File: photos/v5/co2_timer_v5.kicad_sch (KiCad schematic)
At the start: 57 parts, among them J1 BAT1_9V, J2 SOLENOID, J3 AVR-ISP-6 (DNP prod), J4 TM1637_DISPLAY, J5 DC_9-12V, J6 BAT2_9V, SW1 UP, SW2 SET, U1 ATtiny84A-SSU, U2 DS3231M+TRL, U3 MCP1703A-3302E/CB, U4 DRV8871DDAR, U5 TPS3839G30DBZR, U6 SN74LVC1G123DCUR

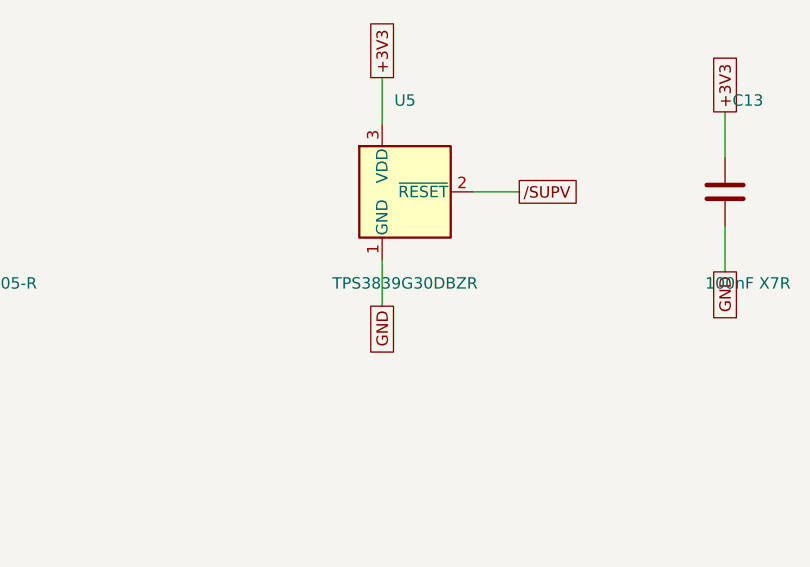
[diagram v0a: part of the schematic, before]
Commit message: docs(co2-timer): v5 fab package and firmware doc refresh
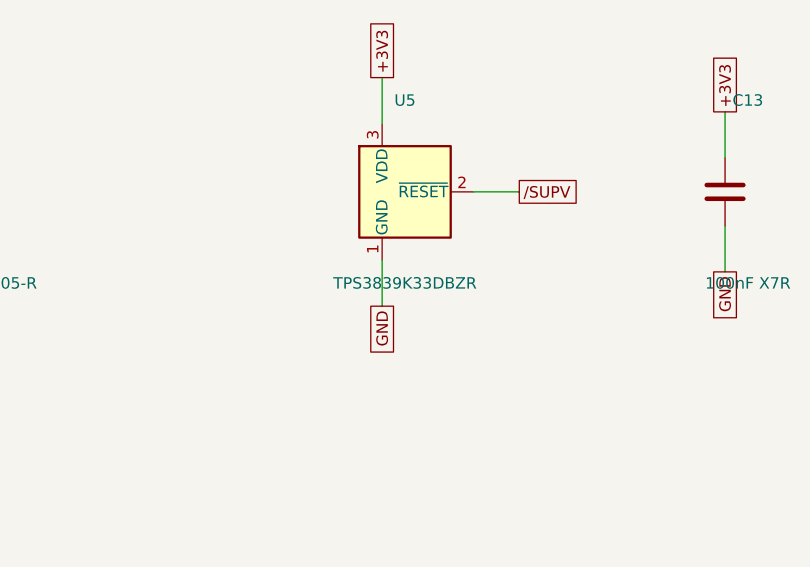
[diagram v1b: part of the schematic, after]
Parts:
- U5: value TPS3839G30DBZR -> TPS3839K33DBZR
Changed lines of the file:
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@@
 			(effects (font (size 1.27 1.27)))
 		)
-		(property "Value" "TPS3839G30DBZR"
+		(property "Value" "TPS3839K33DBZR"
 			(at 345.44 193.04 0)
 			(effects (font (size 1.27 1.27)))

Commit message: co2-timer v5.1: fail-safe redesign + full adversarial remediation
Adversarial review (2026-08-11) found the shipped-for-quote package had a
reversed regulator pinout, a fail-safe chain that could not actuate (supervisor
tripped 3.5 V below bridge UVLO; one-shot mistimed and self-powered; 470 uF
reservoir off by 100x), unmountable C1/SC1/diode footprints, and no valve spec.

Rev 5.1, verified through six adversarial re-review rounds to RELEASE:
- TPS3700 supervisor on VM (180K/10K, trip 7.50 V) + dual SN74LVC1G3157 muxes
  force IN1=0/IN2=1 at the bridge on trip; one-shot/diode-OR deleted
- U3 MCP1703A pad nets corrected everywhere incl. pad oracle and symbol
- C1 -> 2x 1000 uF D10/P5.0 (sag support role); SC1 -> 0.1 F coin (CHP5R5L104R);
  D2/D3 SOD-323 lands; BOM/CPL/netlist/oracle consistent (172/172)
- Firmware safety items 1-11: OSF masks, periodic schedule eval, close-on-reset
  + hop rescue w/ hold release on clean pass, tear-safe complement journal with
  break-count validation, BCD validation, sticky faults, 8.2/8.6 V lockout with
  .noinit latch + sleep-hop release, VM-measured alert classification
  (6,492 B, sha256 64b0808e...4453, compiled arduino-cli/ATTinyCore on gg-wsl)
- Valve: leak-qualified 6 V direct-acting micro latching class, MPN frozen at
  FA T0; dummy loads derived from measured coil; enclosure stays 1554C2GY
- Docs: T0-T8 + G1-G3 test series, ENIG finish, regulated-adapter constraint,
  Bittele 100-unit/5-FA-hold scope, fab package rebuilt with production hex
  + SHA256SUMS
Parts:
- removed C13, C8: 100nF X7R, Capacitor_SMD:C_0603_1608Metric, symbol Device:C
- removed D6: BAT54, Package_TO_SOT_SMD:SOT-23, symbol Device:D_Schottky
- removed U5: TPS3839K33DBZR, Package_TO_SOT_SMD:SOT-23, symbol Power_Supervisor:TPS3839DBZ
- removed U6: SN74LVC1G123DCUR, Package_SO:VSSOP-8_2.3x2mm_P0.5mm, symbol 74xGxx:74LVC1G123
- added C18: 100nF X7R, Capacitor_SMD:C_0603_1608Metric, symbol Device:C
- added C19: 1000uF 25V 105C low-ESR, Capacitor_THT:CP_Radial_D10.0mm_P5.00mm, symbol Device:C_Polarized
- added R17: 100K, Resistor_SMD:R_0603_1608Metric, symbol Device:R
- added R18: 10K, Resistor_SMD:R_0603_1608Metric, symbol Device:R
- added U5: TPS3700DDCR, Package_TO_SOT_SMD:SOT-23-6, symbol co2v5:TPS3700DDCR
- added U6, U7: SN74LVC1G3157DCKR, Package_TO_SOT_SMD:SOT-363_SC-70-6, symbol co2v5:SN74LVC1G3157
- C1: value 470uF 16V 105C low-ESR -> 1000uF 25V 105C low-ESR
- C9: value 470nF X7R -> 100nF X7R
- D2, D3: footprint Package_TO_SOT_SMD:SOT-23 -> Diode_SMD:D_SOD-323
- J5: footprint Connector_BarrelJack:BarrelJack_Horizontal -> co2v5:BarrelJack_CUI_PJ-002A
- R13: value 100K 1% -> 180K 1%
- R16: value 1K -> 10K 1%
- SC1: value 1F 5.5V PB-5R0V105-R -> 0.1F 5.5V CHP5R5L104R-TW; footprint Capacitor_THT:CP_Radial_D10.0mm_P5.00mm -> co2v5:CP_CHP_10x5_P7.50mm
- SW1, SW2: footprint Button_Switch_SMD:SW_SPST_TL3342 -> co2v5:PTS645SM43SMTR92LFS
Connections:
- net OS_CEXT is gone; now on net VM: C9.1
- net +3V3: now also U3.2 (VOUT), C18.1, R18.2, U6.5 (VCC), U7.3 (B1), U7.5 (VCC); no longer R13.2, U3.3 (VOUT)
- net DRV_IN1: now also U6.4 (A); no longer U1.2 (XTAL1/PB0)
- net DRV_IN2: now also U7.4 (A); no longer R16.2
- net DRV_IN2_MCU: now also U7.1 (B2); no longer R16.1
- net GND: now also C9.2, R16.2, C18.2, C19.2, R17.2, U5.2 (GND), U5.4 (INB-), U6.2 (GND), U6.3 (B1), U7.2 (GND)
- net VM: now also R13.1, U3.3 (VIN), C19.1, U5.5 (VDD); no longer U3.2 (VIN)
- net /SUPV renamed /VM_OK
- net /VM_OK: now also R17.1, R18.1, U5.1 (OUTA), U6.6 (S), U7.6 (S)
- removed net OS_RC: C9.2, R13.1
- new net DRV_IN1_MCU: U1.2 (XTAL1/PB0), U6.1 (B2)
- new net VM_DIV: R13.2, R16.1, U5.3 (INA+)
- no-connect marks 2 -> 3
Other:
- note added: "RTC + SUPERCAP BACKUP / VM SUPERVISOR"
- note added: "SOLENOID DRIVER / FAIL-SAFE MUX TAKEOVER"
- note removed: "RTC + SUPERCAP BACKUP / SUPERVISOR"
- note removed: "SOLENOID DRIVER / HW CLOSE ONE-SHOT"
